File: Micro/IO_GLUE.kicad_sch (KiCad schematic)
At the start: 15 parts, among them U21 74HC02, U30 74HC32, U4 74HC00, U5 74HC00, U7 74HC02, U9 74HC08

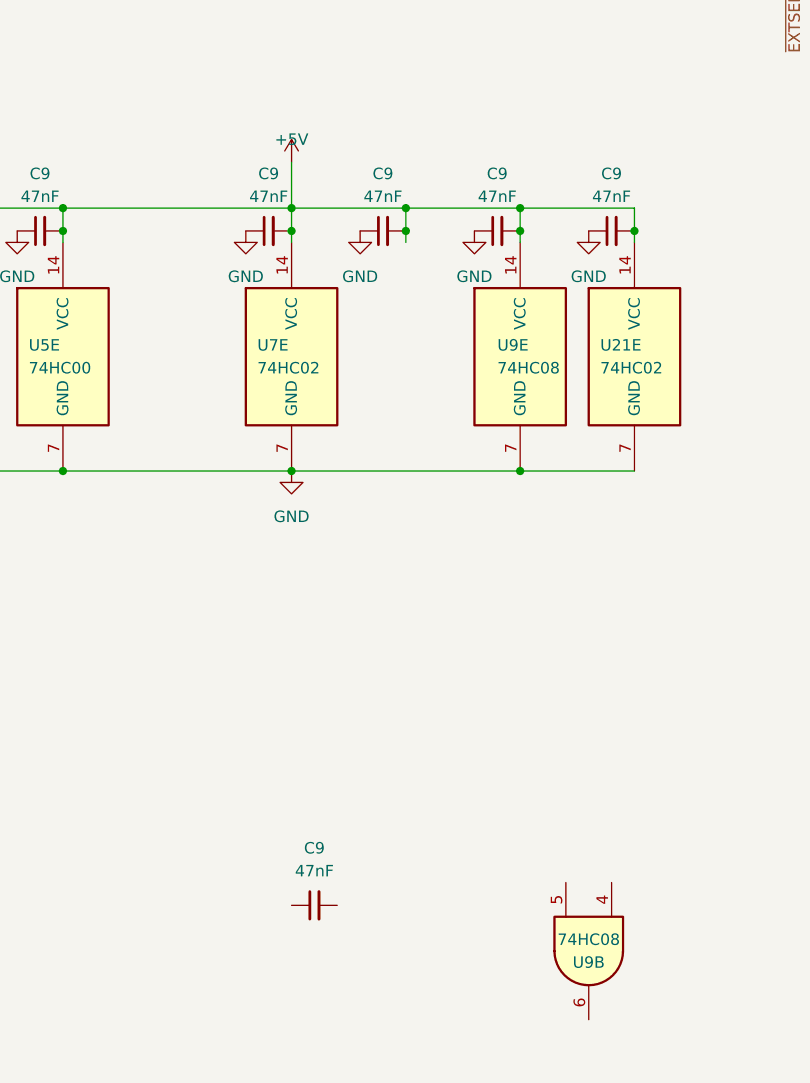
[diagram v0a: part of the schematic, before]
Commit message: Hardware: fixed error in schematic with clock moved dotclock to out 2 (better for jitter) allowed the replacement of 82c54 CPU CLK with CLK 2 moved nmi switch to a more reasonable location
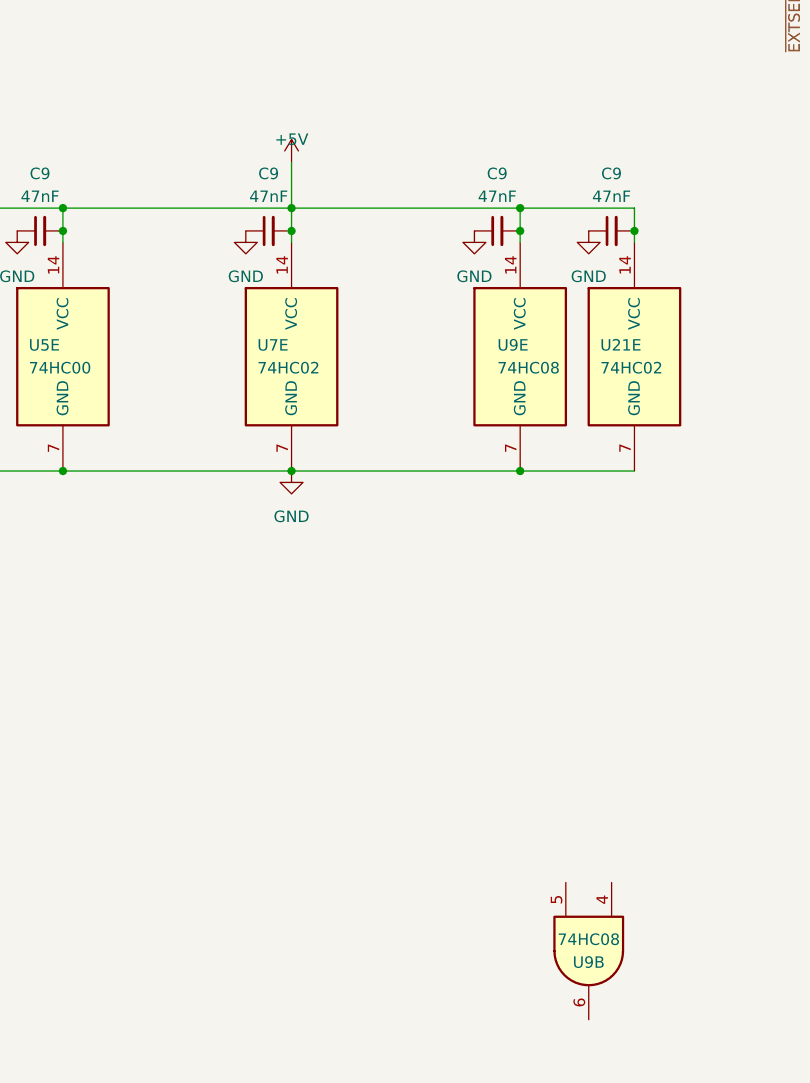
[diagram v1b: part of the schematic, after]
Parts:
- removed C9 (x2): 47nF, Capacitor_SMD:C_0603_1608Metric_Pad1.08x0.95mm_HandSolder, symbol Device:C_Small
- JP11: footprint (none) -> Jumper:SolderJumper-3_P1.3mm_Bridged12_RoundedPad1.0x1.5mm_NumberLabels
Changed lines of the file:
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@@
 (kicad_sch (version 20230121) (generator eeschema)
   (paper "A4")
-  (junction (at 76.2 162.56) (diameter 0) (color 0 0 0 0)
-  )
   (junction (at 101.6 19.05) (diameter 0) (color 0 0 0 0)
   )
@@
   (junction (at 38.1 160.02) (diameter 0) (color 0 0 0 0)
   )
-  (junction (at 76.2 160.02) (diameter 0) (color 0 0 0 0)
-  )
   (junction (at 125.73 67.31) (diameter 0) (color 0 0 0 0)
   )
@@
     (stroke (width 0) (type default))
   )
-  (wire (pts (xy 63.5 160.02) (xy 76.2 160.02))
+  (wire (pts (xy 63.5 160.02) (xy 88.9 160.02))
     (stroke (width 0) (type default))
   )
@@
     (stroke (width 0) (type default))
   )
-  (wire (pts (xy 76.2 160.02) (xy 88.9 160.02))
-    (stroke (width 0) (type default))
-  )
   (wire (pts (xy 45.72 19.05) (xy 101.6 19.05))
     (stroke (width 0) (type default))
@@
     (stroke (width 0) (type default))
   )
-  (wire (pts (xy 76.2 160.02) (xy 76.2 162.56))
-    (stroke (width 0) (type default))
-  )
   (wire (pts (xy 158.75 104.14) (xy 147.32 104.14))
     (stroke (width 0) (type default))
@@
   )
   (wire (pts (xy 101.6 119.38) (xy 101.6 19.05))
-    (stroke (width 0) (type default))
-  )
-  (wire (pts (xy 76.2 162.56) (xy 76.2 163.83))
     (stroke (width 0) (type default))
   )
@@
       (effects (font (size 1.27 1.27)) (justify left))
     )
-    (property "Footprint" "" (at 148.59 63.5 0)
+    (property "Footprint" "Jumper:SolderJumper-3_P1.3mm_Bridged12_RoundedPad1.0x1.5mm_NumberLabels" (at 148.59 63.5 0)
       (effects (font (size 1.27 1.27)) hide)
     )
@@
         (path "/5388c84f-02a4-4503-bb12-5559371e0a41/7bcaf41d-6d3d-4f33-82ee-7daa1c8431e0"
           (reference "JP11") (unit 1)
-        )
-      )
-    )
-  )
-  (symbol (lib_id "power:GND") (at 71.12 162.56 0) (unit 1)
-    (in_bom yes) (on_board yes) (dnp no) (fields_autoplaced)
-    (property "Reference" "#PWR0128" (at 71.12 168.91 0)
-      (effects (font (size 1.27 1.27)) hide)
-    )
-    (property "Value" "GND" (at 71.12 167.64 0)
-      (effects (font (size 1.27 1.27)))
-    )
-    (property "Footprint" "" (at 71.12 162.56 0)
-      (effects (font (size 1.27 1.27)) hide)
-    )
-    (property "Datasheet" "" (at 71.12 162.56 0)
-      (effects (font (size 1.27 1.27)) hide)
-    )
-    (pin "1")
-    (instances
-      (project "Micro"
-        (path "/5388c84f-02a4-4503-bb12-5559371e0a41/0fe507b2-218d-40e0-9689-df5775329c21"
-          (reference "#PWR0128") (unit 1)
-        )
-        (path "/5388c84f-02a4-4503-bb12-5559371e0a41/7bcaf41d-6d3d-4f33-82ee-7daa1c8431e0"
-          (reference "#PWR0182") (unit 1)
         )
       )
@@
     )
   )
-  (symbol (lib_id "Device:C_Small") (at 66.04 237.49 90) (unit 1)
-    (in_bom yes) (on_board yes) (dnp no)
-    (property "Reference" "C9" (at 66.04 231.14 90)
-      (effects (font (size 1.27 1.27)))
-    )
-    (property "Value" "47nF" (at 66.04 233.68 90)
-      (effects (font (size 1.27 1.27)))
-    )
-    (property "Footprint" "Capacitor_SMD:C_0603_1608Metric_Pad1.08x0.95mm_HandSolder" (at 66.04 237.49 0)
-      (effects (font (size 1.27 1.27)) hide)
-    )
-    (property "Datasheet" "~" (at 66.04 237.49 0)
-      (effects (font (size 1.27 1.27)) hide)
-    )
-    (pin "1")
-    (pin "2")
-    (instances
-      (project "Micro"
-        (path "/5388c84f-02a4-4503-bb12-5559371e0a41/0fe507b2-218d-40e0-9689-df5775329c21"
-          (reference "C9") (unit 1)
-        )
-        (path "/5388c84f-02a4-4503-bb12-5559371e0a41/7bcaf41d-6d3d-4f33-82ee-7daa1c8431e0"
-          (reference "C53") (unit 1)
-        )
-      )
-    )
-  )
   (symbol (lib_id "74xx:74HCT00") (at 25.4 176.53 0) (unit 5)
     (in_bom yes) (on_board yes) (dnp no)
@@
         )
       )
-    )
-  )
-  (symbol (lib_id "Device:C_Small") (at 73.66 162.56 90) (unit 1)
-    (in_bom yes) (on_board yes) (dnp no)
-    (property "Reference" "C9" (at 73.66 156.21 90)
-      (effects (font (size 1.27 1.27)))
-    )
-    (property "Value" "47nF" (at 73.66 158.75 90)
-      (effects (font (size 1.27 1.27)))
-    )
-    (property "Footprint" "Capacitor_SMD:C_0603_1608Metric_Pad1.08x0.95mm_HandSolder" (at 73.66 162.56 0)
-      (effects (font (size 1.27 1.27)) hide)
-    )
-    (property "Datasheet" "~" (at 73.66 162.56 0)
-      (effects (font (size 1.27 1.27)) hide)
-    )
-    (pin "1")
-    (pin "2")
-    (instances
-      (project "Micro"
-        (path "/5388c84f-02a4-4503-bb12-5559371e0a41/0fe507b2-218d-40e0-9689-df5775329c21"
-          (reference "C9") (unit 1)
-        )
-        (path "/5388c84f-02a4-4503-bb12-5559371e0a41/7bcaf41d-6d3d-4f33-82ee-7daa1c8431e0"
-          (reference "C55") (unit 1)
-        )
-      )

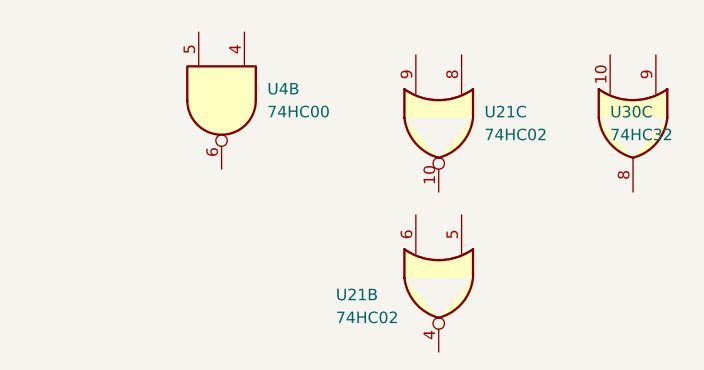
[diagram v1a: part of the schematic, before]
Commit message: Fixed error in TIE LE signal (Logic was inverted, replaced or with nor)
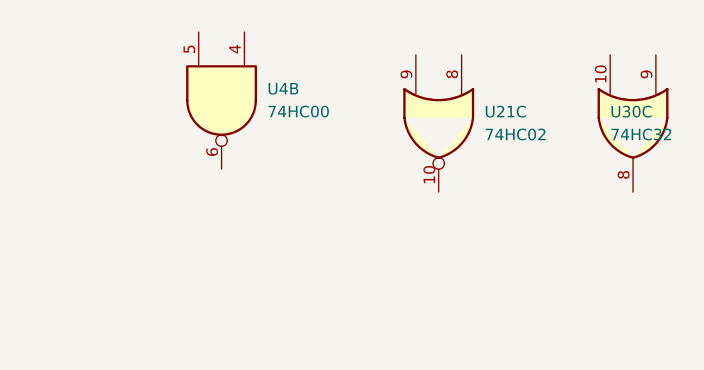
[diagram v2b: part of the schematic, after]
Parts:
- removed unit 2 of U21
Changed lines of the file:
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@@
-    )
-  )
-  (symbol (lib_id "74xx:74HCT02") (at 276.86 257.81 270) (unit 2)
-    (in_bom yes) (on_board yes) (dnp no)
-    (property "Reference" "U21" (at 265.43 259.08 90)
-      (effects (font (size 1.27 1.27)) (justify left))
-    )
-    (property "Value" "74HC02" (at 265.43 261.62 90)
-      (effects (font (size 1.27 1.27)) (justify left))
-    )
-    (property "Footprint" "Package_SO:SOIC-14_3.9x8.7mm_P1.27mm" (at 276.86 257.81 0)
-      (effects (font (size 1.27 1.27)) hide)
-    )
-    (property "Datasheet" "http://www.ti.com/lit/gpn/sn74hct02" (at 276.86 257.81 0)
-      (effects (font (size 1.27 1.27)) hide)
-    )
-    (pin "1")
-    (pin "2")
-    (pin "3")
-    (pin "4")
-    (pin "5")
-    (pin "6")
-    (pin "10")
-    (pin "8")
-    (pin "9")
-    (pin "11")
-    (pin "12")
-    (pin "13")
-    (pin "14")
-    (pin "7")
-    (instances
-      (project "Micro"
-        (path "/5388c84f-02a4-4503-bb12-5559371e0a41/7bcaf41d-6d3d-4f33-82ee-7daa1c8431e0"
-          (reference "U21") (unit 2)
-        )
-      )
     )
   )

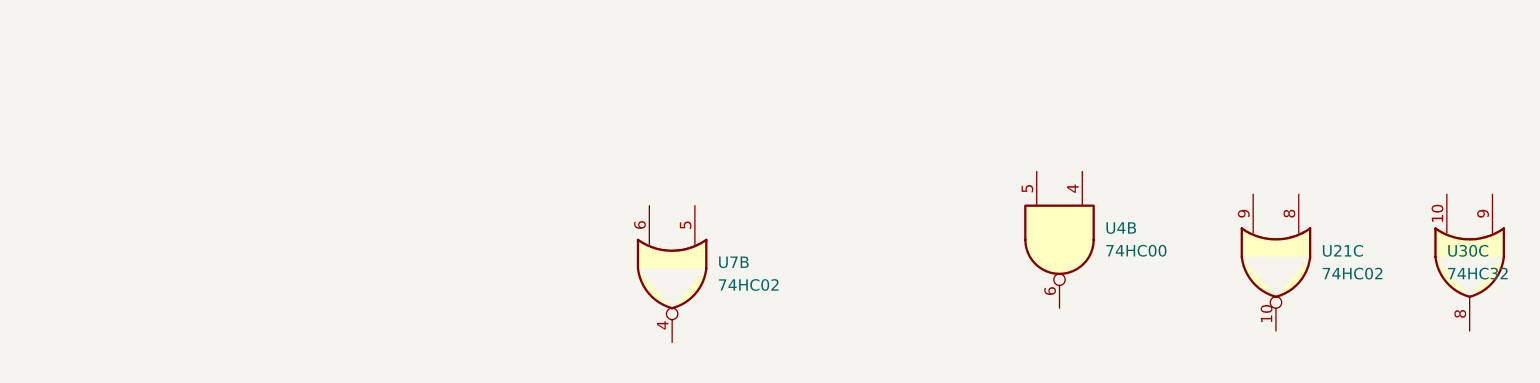
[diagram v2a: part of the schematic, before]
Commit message: Finallized board, added jumpers for debug, added reset to Ext connector other errors fixed
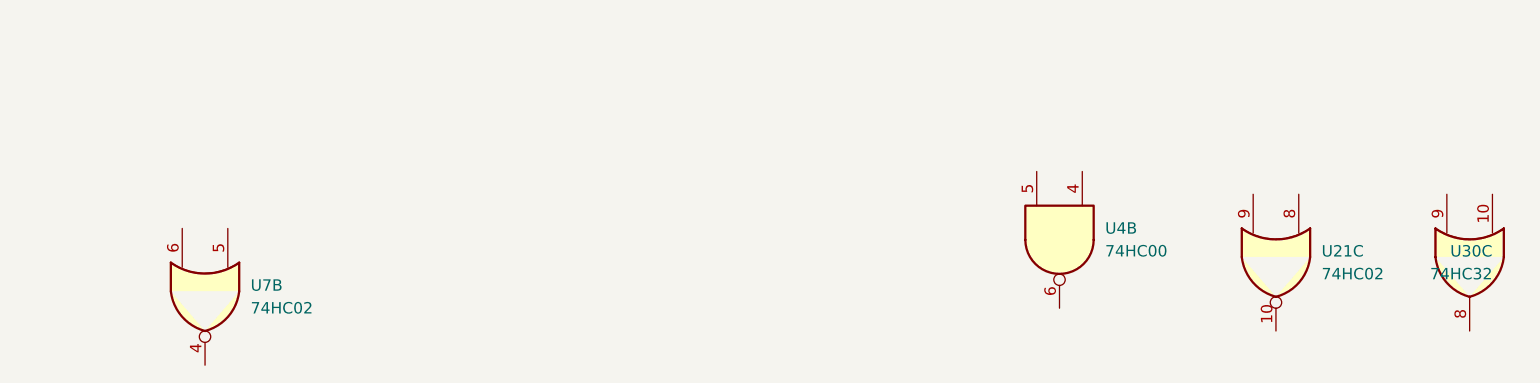
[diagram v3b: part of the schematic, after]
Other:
- moved on the sheet: U30C, U7B
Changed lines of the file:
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@@
     )
   )
-  (symbol (lib_id "74xx:74HCT02") (at 209.55 241.3 270) (unit 2)
+  (symbol (lib_id "74xx:74HCT02") (at 157.48 243.84 270) (unit 2)
     (in_bom yes) (on_board yes) (dnp no) (fields_autoplaced)
-    (property "Reference" "U7" (at 214.63 240.03 90)
+    (property "Reference" "U7" (at 162.56 242.57 90)
       (effects (font (size 1.27 1.27)) (justify left))
     )
-    (property "Value" "74HC02" (at 214.63 242.57 90)
+    (property "Value" "74HC02" (at 162.56 245.11 90)
       (effects (font (size 1.27 1.27)) (justify left))
     )
-    (property "Footprint" "Package_SO:SOIC-14_3.9x8.7mm_P1.27mm" (at 209.55 241.3 0)
+    (property "Footprint" "Package_SO:SOIC-14_3.9x8.7mm_P1.27mm" (at 157.48 243.84 0)
       (effects (font (size 1.27 1.27)) hide)
     )
-    (property "Datasheet" "http://www.ti.com/lit/gpn/sn74hct02" (at 209.55 241.3 0)
+    (property "Datasheet" "http://www.ti.com/lit/gpn/sn74hct02" (at 157.48 243.84 0)
       (effects (font (size 1.27 1.27)) hide)
     )
@@
     )
   )
-  (symbol (lib_id "74xx:74LS32") (at 298.45 240.03 270) (unit 3)
+  (symbol (lib_id "74xx:74LS32") (at 298.45 240.03 90) (mirror x) (unit 3)
     (in_bom yes) (on_board yes) (dnp no)
-    (property "Reference" "U30" (at 295.91 238.76 90)
+    (property "Reference" "U30" (at 300.99 238.76 90)
       (effects (font (size 1.27 1.27)) (justify left))
     )
-    (property "Value" "74HC32" (at 295.91 241.3 90)
+    (property "Value" "74HC32" (at 300.99 241.3 90)
       (effects (font (size 1.27 1.27)) (justify left))
     )
